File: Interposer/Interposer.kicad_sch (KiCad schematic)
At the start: 10 parts, among them J1 Cis_Electrode_In, J10 Trans_Electrode_Out, J11 Trans_Electrode_In, J2 Cis_Electrode_Out

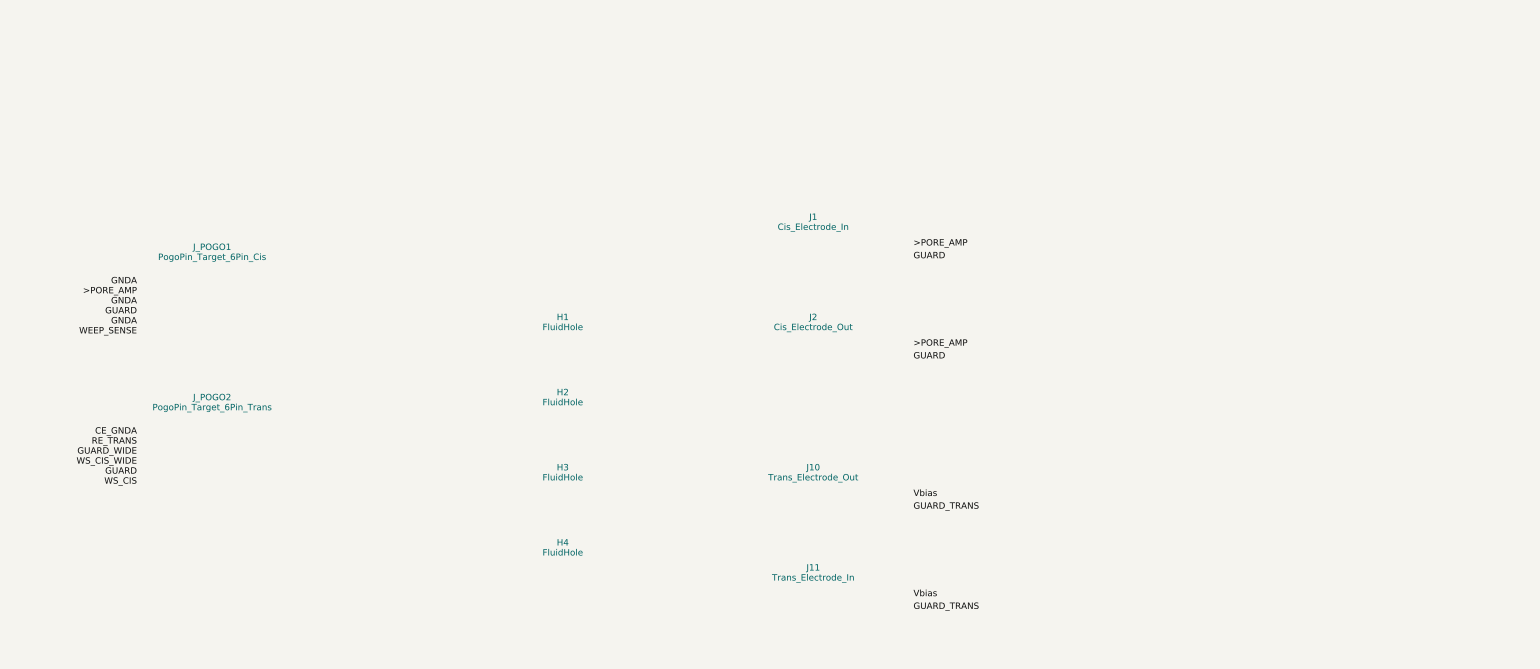
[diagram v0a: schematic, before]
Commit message: feat: implement distributed 2x6 pogo pin map ($36mm span) across Bank A and Bank B
Co-authored-by: google-labs-jules[bot] <161369871+google-labs-jules[bot]@users.noreply.github.com>
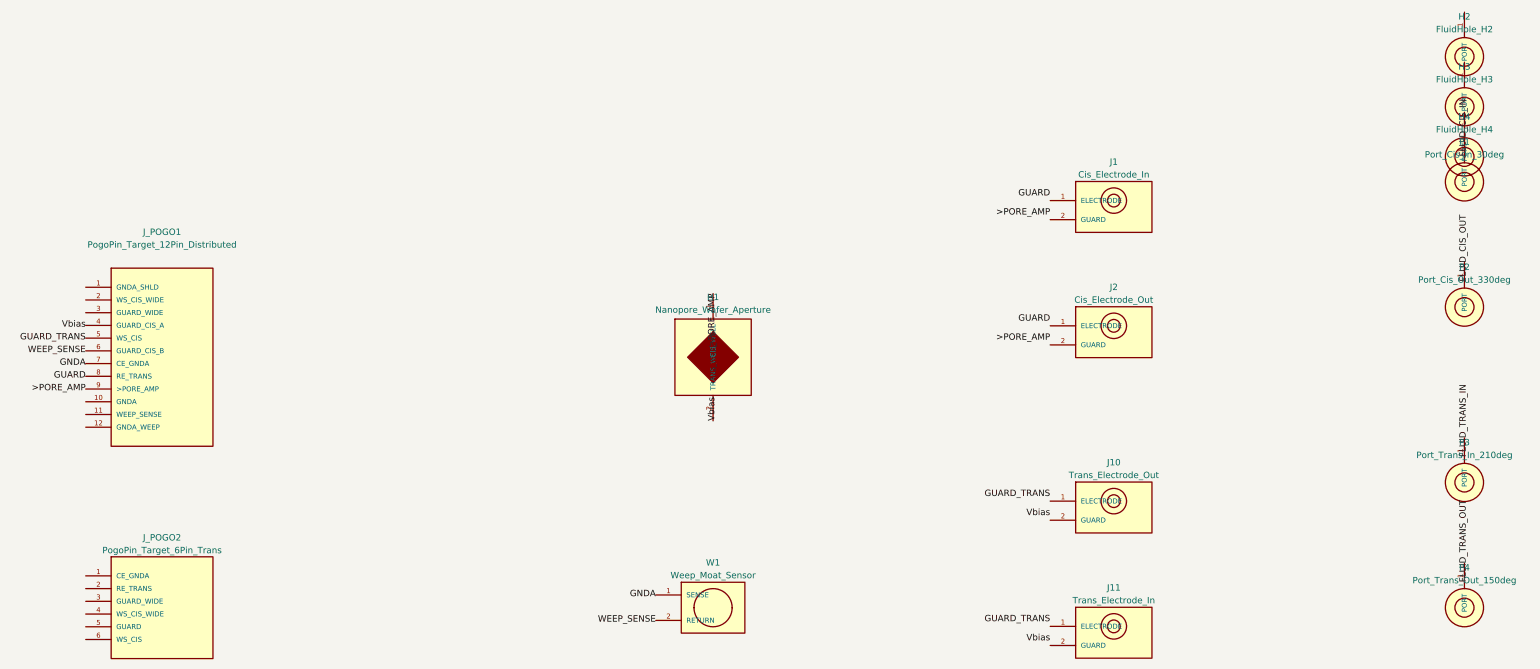
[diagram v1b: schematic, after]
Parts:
- removed H1, H2, H3, H4: FluidHole, MountingHole:MountingHole_2.1mm, symbol Mechanical:MountingHole
- removed J1: Cis_Electrode_In, footprints:Electrode_Guard_Shield, symbol Connector_Generic:Conn_01x02
- removed J10: Trans_Electrode_Out, footprints:Electrode_Guard_Shield, symbol Connector_Generic:Conn_01x02
- removed J11: Trans_Electrode_In, footprints:Electrode_Guard_Shield, symbol Connector_Generic:Conn_01x02
- removed J2: Cis_Electrode_Out, footprints:Electrode_Guard_Shield, symbol Connector_Generic:Conn_01x02
- removed J_POGO1: PogoPin_Target_6Pin_Cis, footprints:PogoPin_Target_6Pin_Cis, symbol Connector_Generic:Conn_01x06
- removed J_POGO2: PogoPin_Target_6Pin_Trans, footprints:PogoPin_Target_6Pin_Trans, symbol Connector_Generic:Conn_01x06
- added H1: Nanopore_Wafer_Aperture, footprints:Nanopore holder_recessed, symbol Interposer:Nanopore_Wafer_Aperture
- added H2: FluidHole_H2, MountingHole:MountingHole_2.1mm, symbol Interposer:Fluidic_Port_PassThrough
- added H3: FluidHole_H3, MountingHole:MountingHole_2.1mm, symbol Interposer:Fluidic_Port_PassThrough
- added H4: FluidHole_H4, MountingHole:MountingHole_2.1mm, symbol Interposer:Fluidic_Port_PassThrough
- added J1: Cis_Electrode_In, footprints:Electrode_Guard_Shield, symbol Interposer:Electrode_Guard_Shield
- added J10: Trans_Electrode_Out, footprints:Electrode_Guard_Shield, symbol Interposer:Electrode_Guard_Shield
- added J11: Trans_Electrode_In, footprints:Electrode_Guard_Shield, symbol Interposer:Electrode_Guard_Shield
- added J2: Cis_Electrode_Out, footprints:Electrode_Guard_Shield, symbol Interposer:Electrode_Guard_Shield
- added J_POGO1: PogoPin_Target_12Pin_Distributed, footprints:PogoPin_Target_12Pin_Distributed, symbol Interposer:PogoPin_Target_12Pin_Distributed
- added J_POGO2: PogoPin_Target_6Pin_Trans, footprints:PogoPin_Target_6Pin_Trans, symbol Interposer:PogoPin_Target_6Pin_Trans
- added P1: Port_Cis_In_30deg, symbol Interposer:Fluidic_Port_PassThrough
- added P2: Port_Cis_Out_330deg, symbol Interposer:Fluidic_Port_PassThrough
- added P3: Port_Trans_In_210deg, symbol Interposer:Fluidic_Port_PassThrough
- added P4: Port_Trans_Out_150deg, symbol Interposer:Fluidic_Port_PassThrough
- added W1: Weep_Moat_Sensor, symbol Interposer:Weep_Moat_Sensor
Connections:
- net >PORE_AMP: now also H1.1 (CIS_WELL), J_POGO1.9 (>PORE_AMP)
- net GNDA: now also J_POGO1.7 (CE_GNDA), W1.1 (SENSE)
- net GUARD: now also J_POGO1.8 (RE_TRANS)
- net GUARD_TRANS: now also J_POGO1.5 (WS_CIS)
- net Vbias: now also H1.2 (TRANS_WELL), J_POGO1.4 (GUARD_CIS_A)
- net WEEP_SENSE: now also J_POGO1.6 (GUARD_CIS_B), W1.2 (RETURN)
